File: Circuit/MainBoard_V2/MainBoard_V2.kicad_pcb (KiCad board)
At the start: 2 copper layers, 56 x 65 mm, 122 parts, among them J1 Conn_01x02, J10 Conn_01x03, J11 Conn_01x03, J12 Conn_01x03, J13 Conn_01x04, J14 Conn_01x04, J15 Conn_01x04, J16 Conn_01x04, J17 Conn_01x04, J18 Conn_01x02, J19 Conn_01x02, J2 Conn_01x02, J20 Conn_01x02, J21 Conn_01x02, J3 Conn_01x02, J4 Conn_01x04, J5 Conn_01x02, J6 Conn_01x02, J7 Conn_01x02, J8 Conn_01x07, J9 Raspberry_Pi_2_3, Q1 Q_PMOS_GDS, Q2 Q_PMOS_GDS, Q3 BSS138, Q4 BSS138, Q5 BSS138, Q6 BSS138, Q7 BSS138, SW1 SW_Push, SW2 SW_Push, SW3 SW_Push, SW4 SW_Slide_DPDT, SW5 SW_Slide_DPDT, U1 STM32F446RETx, U2 LM1117MP-3.3, U3 MPU-6050, Y1 CSTNE16M0V530000R0

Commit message: V2完成
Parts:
- added C19: 10u, Capacitor_SMD:C_0805_2012Metric, B.Cu at (119.0, 149.8)
- added R37: 10, Resistor_SMD:R_0603_1608Metric, F.Cu at (107.5, 144.5)
- C6: footprint Capacitor_THT:CP_Radial_D5.0mm_P2.00mm -> Capacitor_THT:CP_Radial_D6.3mm_P2.50mm; moved to B.Cu
- C7: footprint Capacitor_THT:CP_Radial_D5.0mm_P2.00mm -> Capacitor_THT:CP_Radial_D6.3mm_P2.50mm
- moved TP9 1.27 mm to (112.8, 127.0)
- moved TP8 1.03 mm to (111.0, 127.0)
- moved TP7 0.79 mm to (109.2, 127.0)
- moved C7 0.50 mm to (117.0, 129.9)
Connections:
- J4 pad 3: TX3 -> LIDAR_OUT
- MD1 pad 1: Net-(MD1-~{ON}/OFF_CONTROL) -> GND
- MD1 pad 5: unconnected-(MD1-SENSE-Pad5) -> +5V
- R4 pad 2: Net-(MD1-~{ON}/OFF_CONTROL) -> GND
- R9 pad 1: GND -> Net-(R37-Pad1)
- U1 pad 44: TRIG2 -> LIDAR_OUT
- U1 pad 45: ECHO1 -> TRIG2
- U1 pad 50: TRIG1 -> ECHO1
- U1 pad 51: TX3 -> TRIG1
- U1 pad 55: unconnected-(U1-PB3-Pad55) -> BUZZER
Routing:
- net BUZZER: track 0.00 -> 22.9 mm, vias 0 -> 1
- net LIDAR_OUT: track 0.00 -> 16.2 mm, vias 0 -> 1
- net TX3: track 6.45 -> 0.00 mm
- net +3V3: track 219.3 -> 224.8 mm
- net +5V: track 141.1 -> 144.9 mm
- net GND: track 17.6 -> 20.9 mm, vias 216 -> 224
- net Net-(MD1-~{ON}/OFF_CONTROL): track 3.34 -> 0.00 mm
- net Net-(R37-Pad1): track 0.00 -> 1.60 mm
- net TRIG1: track 10.7 -> 11.4 mm
- net ECHO1: track 12.7 -> 13.1 mm, vias 0 -> 2
- net GNDP: vias 23 -> 28
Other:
- board text added: "MainBoard V2"
- board text removed: "MainBoard V1"

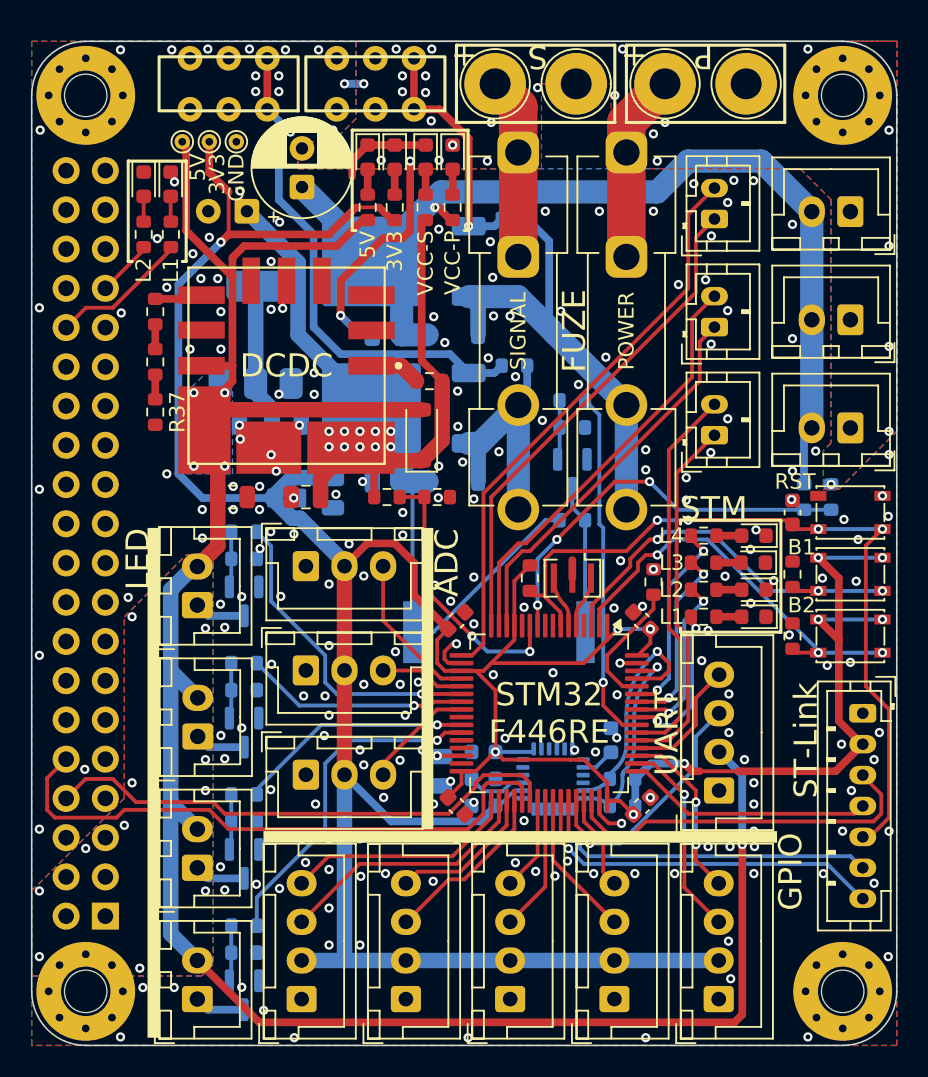
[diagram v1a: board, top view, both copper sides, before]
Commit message: Update MainBoard V2 production files
- Updated BOM to include additional capacitors (C20, C21) with increased quantities.
- Added new designators for capacitors C20 and C21 in designators.csv.
- Modified netlist.ipc to reflect changes in the circuit layout, including new connections and adjustments to existing vias.
- Adjusted positions.csv for precise component placement, including minor adjustments to several components' coordinates.
- Added a backup of the MainBoard V2 design from May 7, 2026.
- Updated the MainBoard V2 production zip file with the latest design files.
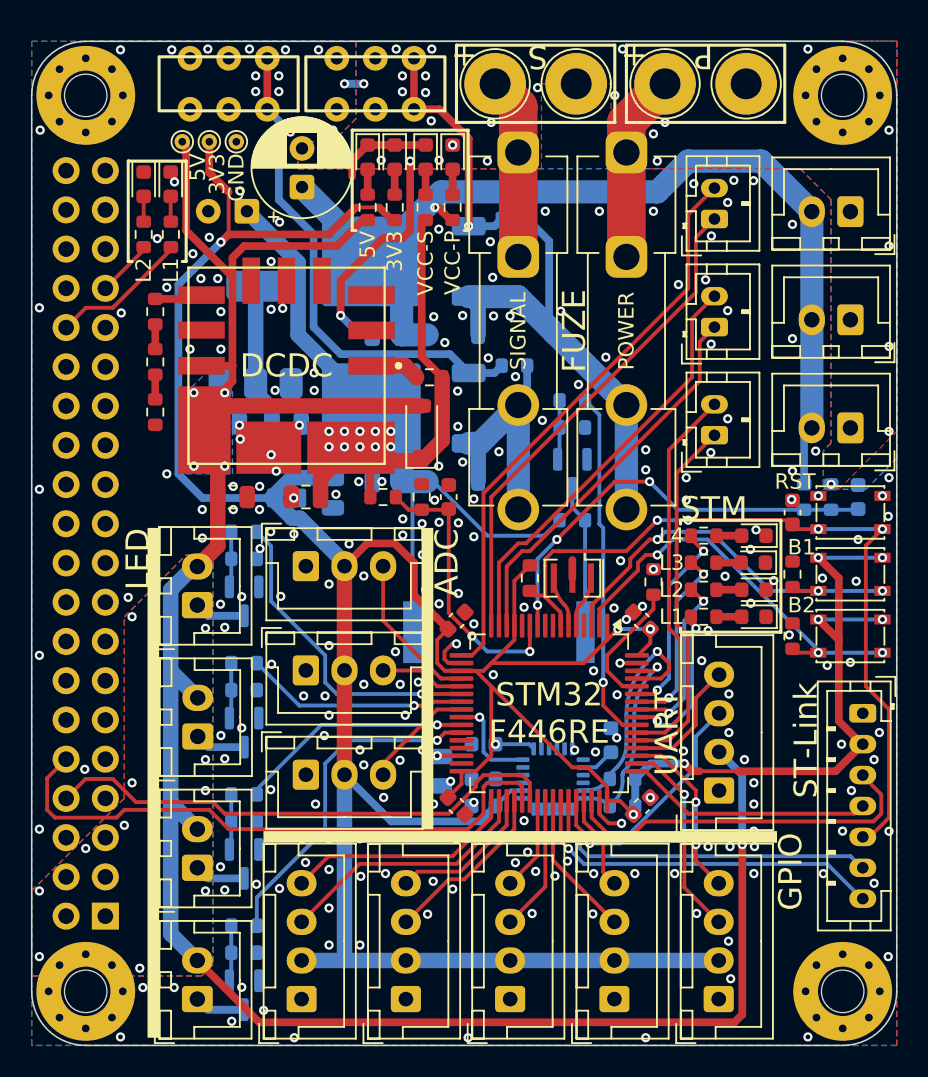
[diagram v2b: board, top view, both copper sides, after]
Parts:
- added C20: 0.1uf, Capacitor_SMD:C_0603_1608Metric, F.Cu at (126.5, 150.0)
- added C21: 0.1uf, Capacitor_SMD:C_0603_1608Metric, B.Cu at (153.0, 150.0)
- moved R19 1.00 mm to (124.8, 150.0), turned to -90 degrees
- moved C15 0.50 mm to (128.8, 166.0)
- moved D1 0.25 mm to (124.8, 145.8)
- moved R18 0.25 mm to (122.2, 150.0)
- moved R4 0.25 mm to (125.2, 142.2)
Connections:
- U1 pad 25: unconnected-(U1-PC5-Pad25) -> INT
- U3 pad 12: unconnected-(U3-INT-Pad12) -> INT
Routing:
- net INT: track 0.00 -> 6.29 mm, vias 0 -> 1
- net GND: track 20.9 -> 16.9 mm, vias 224 -> 239
- net VCC: track 75.3 -> 73.1 mm
- net +3V3: track 224.8 -> 226.7 mm
- net VOLTAGEP: track 26.2 -> 27.9 mm
- net VOLTAGE: track 17.7 -> 18.5 mm

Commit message: ゾーン修正
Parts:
- added C22: 10u, Capacitor_SMD:C_0805_2012Metric, B.Cu at (106.5, 170.2)
- added C23: 0.1uf, Capacitor_SMD:C_0603_1608Metric, B.Cu at (146.2, 167.8)
- added C24: 10u, Capacitor_SMD:C_0805_2012Metric, B.Cu at (107.5, 181.2)
- added C25: 10u, Capacitor_SMD:C_0805_2012Metric, B.Cu at (151.2, 147.8)
- moved C5 10.9 mm to (119.5, 129.0), turned to -90 degrees
- moved R7 5.86 mm to (133.3, 137.2), turned to 90 degrees
- moved C21 0.56 mm to (153.2, 150.5)
- moved R20 0.56 mm to (149.2, 150.5)
- moved R21 0.56 mm to (151.5, 150.5)
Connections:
- C5 pad 1: VCCP -> GNDP
- C5 pad 2: GNDP -> VCCP
- J9 pad 12: unconnected-(J9-GPIO18/PWM0-Pad12) -> BUZZER
- J9 pad 32: RAS_LED1 -> unconnected-(J9-PWM0/GPIO12-Pad32)
- J9 pad 35: unconnected-(J9-GPIO19/MISO1-Pad35) -> RAS_LED1
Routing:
- net VCCP: track 65.8 -> 4.59 mm
- net BUZZER: track 22.9 -> 60.6 mm, vias 1 -> 2
- net Net-(D3-K): track 30.2 -> 0.00 mm
- net GNDP: track 15.2 -> 0.00 mm, vias 28 -> 31
- net Net-(D2-K): track 16.5 -> 2.78 mm
- net +5V: track 145.0 -> 132.2 mm, vias 16 -> 18
- net Net-(Q2-G): track 15.6 -> 22.0 mm
- net RAS_LED1: track 9.03 -> 4.98 mm
- net GND: vias 239 -> 214
- added copper zone on B.Cu, net Net-(D2-K)
- added copper zone on B.Cu, net Net-(D3-K)
- added copper zone on B.Cu, net VCCP

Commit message: 発注
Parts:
- added C26: 10u, Capacitor_SMD:C_0805_2012Metric, B.Cu at (120.6, 173.5)
- U3: footprint Sensor_Motion:InvenSense_QFN-24_4x4mm_P0.5mm -> Package_DFN_QFN:QFN-24-1EP_4x4mm_P0.5mm_EP2.15x2.15mm
- moved R7 3.14 mm to (130.2, 137.8)
- moved C5 0.50 mm to (119.5, 128.5)
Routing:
- net +5V: track 132.2 -> 100.4 mm, vias 18 -> 76
- net +BATTP: track 12.2 -> 0.00 mm
- net +BATT: track 11.8 -> 0.00 mm
- net Net-(Q2-G): track 22.0 -> 19.1 mm
- net Net-(D2-K): track 2.78 -> 0.00 mm
- net VOLTAGE: track 18.5 -> 16.1 mm
- net +3V3: track 226.7 -> 227.5 mm
- net GND: track 16.9 -> 17.8 mm, vias 214 -> 315
- net Net-(Q1-G): track 32.2 -> 31.5 mm
- net VCC: track 73.0 -> 73.6 mm, vias 10 -> 18
- net VCCP: track 4.59 -> 4.03 mm
- net GNDP: vias 31 -> 34
- added copper zone on F.Cu, net +BATT
- added copper zone on F.Cu, net +BATTP
